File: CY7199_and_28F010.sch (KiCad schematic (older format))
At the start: 10 parts, among them U1 28F010, U10 74LS04, U11 74LS04, U2 28F010, U3 CY7C199, U4 CY7C199, U5 CY7C199, U6 CY7C199, U7 PAL16L8, U9 74LS04

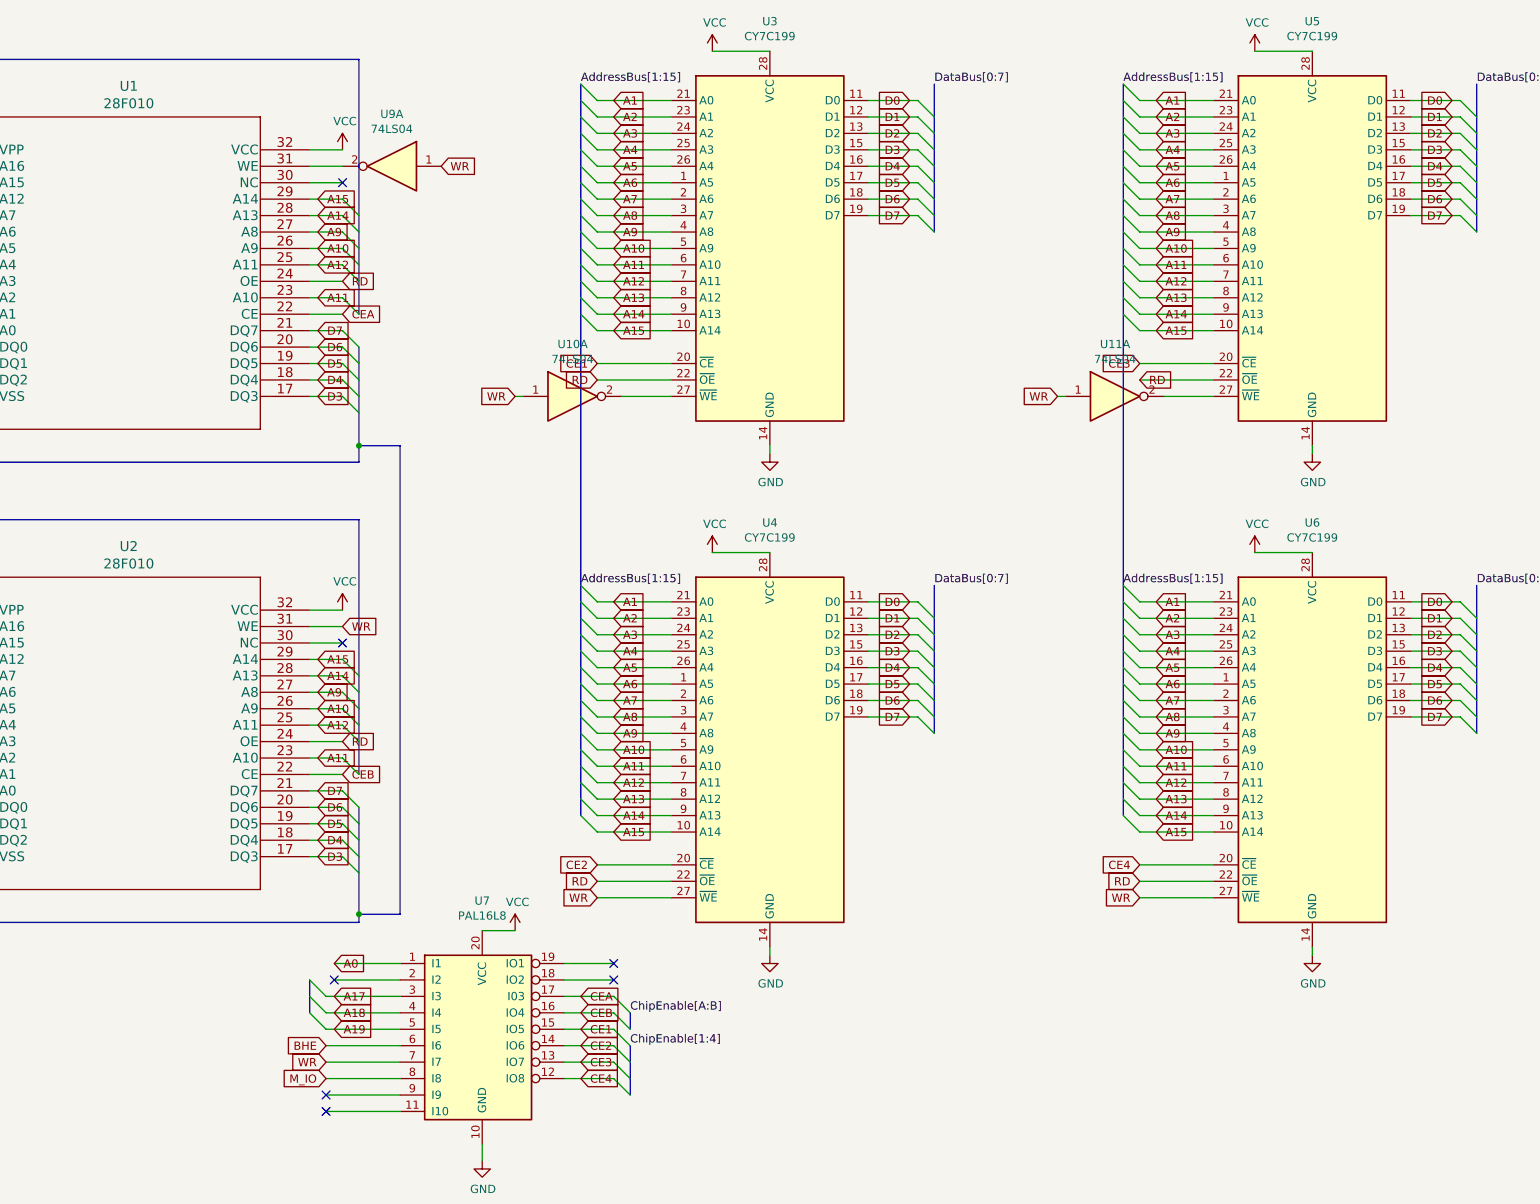
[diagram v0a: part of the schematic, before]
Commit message: tweeked cy7119_and_28f010.sch
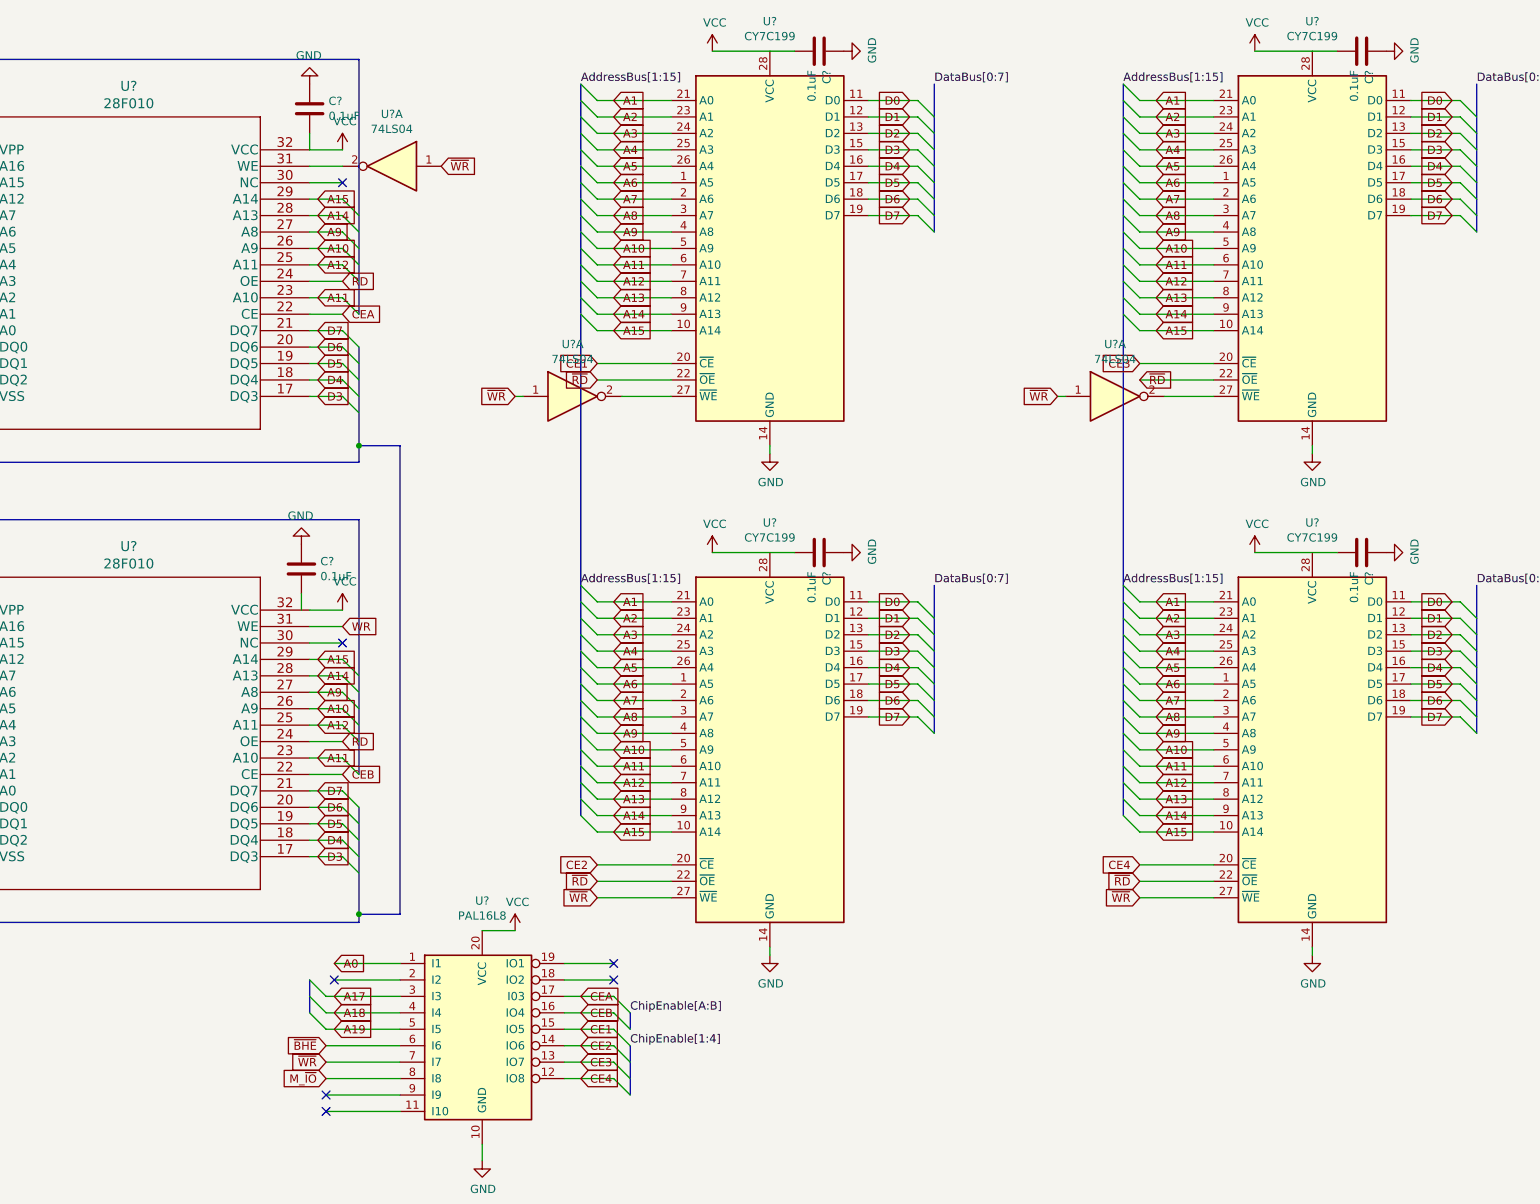
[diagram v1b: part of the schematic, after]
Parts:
- added C? (x6): 0.1uF, symbol Device:C
- renumbered U3 to U?, U7 to U?, U4 to U?, U2 to U?, U1 to U?, U5 to U?, U6 to U?, U11 to U?, U10 to U?, U9 to U?
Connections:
- net GND: now also C?.1, C?.1, C?.1, C?.1, C?.1, C?.1
- net RD: no longer U?.22 (~OE~), U?.22 (~OE~), U?.22 (~OE~), U?.22 (~OE~)
- net VCC: now also C?.2, C?.2, C?.2, C?.2, C?.2
- net WR: no longer U?.1, U?.1, U?.1, U?.27 (~WE~), U?.27 (~WE~), U?.7 (I7)
- net BHE renamed ~BHE
- net M_IO renamed M_~IO
- new net ~RD: U?.22 (~OE~), U?.22 (~OE~), U?.22 (~OE~), U?.22 (~OE~)
- new net ~WR: U?.1, U?.1, U?.1, U?.27 (~WE~), U?.27 (~WE~), U?.7 (I7)

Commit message: tweaked a few things
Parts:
- gave numbers to parts that had none: 16
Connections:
- net RD is gone; now on net ~RD: U601.24 (OE), U602.24 (OE)
- net WR is gone; now on net ~WR: U602.31 (WE)
- net VCC: now also C601.2
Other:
- moved on the sheet: C601
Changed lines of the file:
@@
 DataBus[0:7]
 $Comp
-L power:VCC #PWR?
+L power:VCC #PWR0157
 U 1 1 60912D5A
 P 3600 4250
-F 0 "#PWR?" H 3600 4100 50  0001 C CNN
+F 0 "#PWR0157" H 3600 4100 50  0001 C CNN
 F 1 "VCC" H 3615 4423 50  0000 C CNN
 F 2 "" H 3600 4250 50  0001 C CNN
@@
 $EndComp
 $Comp
-L power:GND #PWR?
+L power:GND #PWR0158
 U 1 1 609136CA
 P 1000 5750
-F 0 "#PWR?" H 1000 5500 50  0001 C CNN
+F 0 "#PWR0158" H 1000 5500 50  0001 C CNN
 F 1 "GND" H 1005 5577 50  0000 C CNN
 F 2 "" H 1000 5750 50  0001 C CNN
@@
 DataBus[0:7]
 $Comp
-L power:VCC #PWR?
+L power:VCC #PWR0159
 U 1 1 60989210
 P 3600 1450
-F 0 "#PWR?" H 3600 1300 50  0001 C CNN
+F 0 "#PWR0159" H 3600 1300 50  0001 C CNN
 F 1 "VCC" H 3615 1623 50  0000 C CNN
 F 2 "" H 3600 1450 50  0001 C CNN
@@
 $EndComp
 $Comp
-L power:GND #PWR?
+L power:GND #PWR0160
 U 1 1 60989216
 P 1000 2950
-F 0 "#PWR?" H 1000 2700 50  0001 C CNN
+F 0 "#PWR0160" H 1000 2700 50  0001 C CNN
 F 1 "GND" H 1005 2777 50  0000 C CNN
 F 2 "" H 1000 2950 50  0001 C CNN
@@
 	6200 6300 6200 6350
 $Comp
-L power:GND #PWR?
+L power:GND #PWR0161
 U 1 1 60C13B52
 P 6200 3300
-F 0 "#PWR?" H 6200 3050 50  0001 C CNN
+F 0 "#PWR0161" H 6200 3050 50  0001 C CNN
 F 1 "GND" H 6205 3127 50  0000 C CNN
 F 2 "" H 6200 3300 50  0001 C CNN
@@
 $EndComp
 $Comp
-L power:GND #PWR?
+L power:GND #PWR0162
 U 1 1 60C14372
 P 6200 6350
-F 0 "#PWR?" H 6200 6100 50  0001 C CNN
+F 0 "#PWR0162" H 6200 6100 50  0001 C CNN
 F 1 "GND" H 6205 6177 50  0000 C CNN
 F 2 "" H 6200 6350 50  0001 C CNN
@@
 	6200 850  5850 850
 $Comp
-L power:VCC #PWR?
+L power:VCC #PWR0163
 U 1 1 60C49E31
 P 5850 850
-F 0 "#PWR?" H 5850 700 50  0001 C CNN
+F 0 "#PWR0163" H 5850 700 50  0001 C CNN
 F 1 "VCC" H 5865 1023 50  0000 C CNN
 F 2 "" H 5850 850 50  0001 C CNN
@@
 $EndComp
 $Comp
-L power:VCC #PWR?
+L power:VCC #PWR0164
 U 1 1 60C4A9F7
 P 5850 3900
-F 0 "#PWR?" H 5850 3750 50  0001 C CNN
+F 0 "#PWR0164" H 5850 3750 50  0001 C CNN
 F 1 "VCC" H 5865 4073 50  0000 C CNN
 F 2 "" H 5850 3900 50  0001 C CNN
@@
 	9500 6300 9500 6350
 $Comp
-L power:GND #PWR?
+L power:GND #PWR0165
 U 1 1 60D25A8A
 P 9500 3300
-F 0 "#PWR?" H 9500 3050 50  0001 C CNN
+F 0 "#PWR0165" H 9500 3050 50  0001 C CNN
 F 1 "GND" H 9505 3127 50  0000 C CNN
 F 2 "" H 9500 3300 50  0001 C CNN
@@
 $EndComp
 $Comp
-L power:GND #PWR?
+L power:GND #PWR0166
 U 1 1 60D25A90
 P 9500 6350
-F 0 "#PWR?" H 9500 6100 50  0001 C CNN
+F 0 "#PWR0166" H 9500 6100 50  0001 C CNN
 F 1 "GND" H 9505 6177 50  0000 C CNN
 F 2 "" H 9500 6350 50  0001 C CNN
@@
 	9500 850  9150 850
 $Comp
-L power:VCC #PWR?
+L power:VCC #PWR0167
 U 1 1 60D25A98
 P 9150 850
-F 0 "#PWR?" H 9150 700 50  0001 C CNN
+F 0 "#PWR0167" H 9150 700 50  0001 C CNN
 F 1 "VCC" H 9165 1023 50  0000 C CNN
 F 2 "" H 9150 850 50  0001 C CNN
@@
 $EndComp
 $Comp
-L power:VCC #PWR?
+L power:VCC #PWR0168
 U 1 1 60D25A9E
 P 9150 3900
-F 0 "#PWR?" H 9150 3750 50  0001 C CNN
+F 0 "#PWR0168" H 9150 3750 50  0001 C CNN
 F 1 "VCC" H 9165 4073 50  0000 C CNN
 F 2 "" H 9150 3900 50  0001 C CNN
@@
 ~RD
 Text GLabel 3600 2250 2    50   Input ~ 0
-RD
+~RD
 Text GLabel 3600 5050 2    50   Input ~ 0
-RD
+~RD
 NoConn ~ 1000 1450
 NoConn ~ 1000 4250
 $Comp
-L Memory_RAM:CY7C199 U?
+L Memory_RAM:CY7C199 U610
 U 1 1 60D25A72
 P 9500 5100
-F 0 "U?" H 9500 6481 50  0000 C CNN
+F 0 "U610" H 9500 6481 50  0000 C CNN
 F 1 "CY7C199" H 9500 6390 50  0000 C CNN
 F 2 "" H 9500 5100 50  0001 C CNN
@@
 $EndComp
 $Comp
-L Memory_RAM:CY7C199 U?
+L Memory_RAM:CY7C199 U609
 U 1 1 60D259E8
 P 9500 2050
-F 0 "U?" H 9500 3431 50  0000 C CNN
+F 0 "U609" H 9500 3431 50  0000 C CNN
 F 1 "CY7C199" H 9500 3340 50  0000 C CNN
 F 2 "" H 9500 2050 50  0001 C CNN
@@
 $EndComp
 $Comp
-L Memory_RAM:CY7C199 U?
+L Memory_RAM:CY7C199 U607
 U 1 1 6081B573
 P 6200 5100
-F 0 "U?" H 6200 6481 50  0000 C CNN
+F 0 "U607" H 6200 6481 50  0000 C CNN
 F 1 "CY7C199" H 6200 6390 50  0000 C CNN
 F 2 "" H 6200 5100 50  0001 C CNN
@@
 $EndComp
 $Comp
-L Memory_RAM:CY7C199 U?
+L Memory_RAM:CY7C199 U606
 U 1 1 6078FC09
 P 6200 2050
-F 0 "U?" H 6200 3431 50  0000 C CNN
+F 0 "U606" H 6200 3431 50  0000 C CNN
 F 1 "CY7C199" H 6200 3340 50  0000 C CNN
 F 2 "" H 6200 2050 50  0001 C CNN
@@
 $EndComp
 $Comp
-L 28F010:28F010 U?
+L 28F010:28F010 U602
 U 1 1 608BE934
 P 1200 4250
-F 0 "U?" H 2300 4637 60  0000 C CNN
+F 0 "U602" H 2300 4637 60  0000 C CNN
 F 1 "28F010" H 2300 4531 60  0000 C CNN
 F 2 "28F010" H 2300 4490 60  0001 C CNN
@@
 $EndComp
 $Comp
-L 28F010:28F010 U?
+L 28F010:28F010 U601
 U 1 1 609891ED
 P 1200 1450
-F 0 "U?" H 2300 1837 60  0000 C CNN
+F 0 "U601" H 2300 1837 60  0000 C CNN
 F 1 "28F010" H 2300 1731 60  0000 C CNN
 F 2 "28F010" H 2300 1690 60  0001 C CNN
@@
 	4950 6500 5250 6500
 $Comp
-L power:VCC #PWR?
+L power:VCC #PWR0169
 U 1 1 60C816AC
 P 4650 6200
-F 0 "#PWR?" H 4650 6050 50  0001 C CNN
+F 0 "#PWR0169" H 4650 6050 50  0001 C CNN
 F 1 "VCC" H 4665 6373 50  0000 C CNN
 F 2 "" H 4650 6200 50  0001 C CNN
@@
 	4450 6200 4650 6200
 $Comp
-L power:GND #PWR?
+L power:GND #PWR0170
 U 1 1 609E86E1
 P 4450 7600
-F 0 "#PWR?" H 4450 7350 50  0001 C CNN
+F 0 "#PWR0170" H 4450 7350 50  0001 C CNN
 F 1 "GND" H 4455 7427 50  0000 C CNN
 F 2 "" H 4450 7600 50  0001 C CNN
@@
 	4450 7500 4450 7600
 $Comp
-L Logic_Programmable:PAL16L8 U?
+L Logic_Programmable:PAL16L8 U604
 U 1 1 6079CE46
 P 4450 6900
-F 0 "U?" H 4450 7781 50  0000 C CNN
+F 0 "U604" H 4450 7781 50  0000 C CNN
 F 1 "PAL16L8" H 4450 7690 50  0000 C CNN
 F 2 "" H 4450 6900 50  0001 C CNN
@@
 	5600 2950 5300 2950
 $Comp
-L 74xx:74LS04 U?
+L 74xx:74LS04 U605
 U 1 1 60EB960C
 P 5000 2950
-F 0 "U?" H 5000 3267 50  0000 C CNN
+F 0 "U605" H 5000 3267 50  0000 C CNN
 F 1 "74LS04" H 5000 3176 50  0000 C CNN
 F 2 "" H 5000 2950 50  0001 C CNN
@@
 D7
 Text GLabel 3600 4350 2    50   Input ~ 0
-WR
+~WR
 Text GLabel 8550 4200 2    50   Input ~ 0
 A1
@@
 	8000 2950 7950 2950
 $Comp
-L 74xx:74LS04 U?
+L 74xx:74LS04 U608
 U 1 1 60DAFE04
 P 8300 2950
-F 0 "U?" H 8300 3267 50  0000 C CNN
+F 0 "U608" H 8300 3267 50  0000 C CNN
 F 1 "74LS04" H 8300 3176 50  0000 C CNN
 F 2 "" H 8300 2950 50  0001 C CNN
@@
 $EndComp
 $Comp
-L 74xx:74LS04 U?
+L 74xx:74LS04 U603
 U 1 1 60F155ED
 P 3900 1550
-F 0 "U?" H 3900 1867 50  0000 C CNN
+F 0 "U603" H 3900 1867 50  0000 C CNN
 F 1 "74LS04" H 3900 1776 50  0000 C CNN
 F 2 "" H 3900 1550 50  0001 C CNN
@@
 	6200 850  6350 850
 $Comp
-L Device:C C?
+L Device:C C603
 U 1 1 60ACE147
 P 6500 850
-F 0 "C?" H 6615 896 50  0000 L CNN
+F 0 "C603" H 6615 896 50  0000 L CNN
 F 1 "0.1uF" H 6615 805 50  0000 L CNN
 F 2 "" H 6538 700 50  0001 C CNN
@@
 $EndComp
 $Comp
-L power:GND #PWR?
+L power:GND #PWR0171
 U 1 1 60ACE14D
 P 6650 850
-F 0 "#PWR?" H 6650 600 50  0001 C CNN
+F 0 "#PWR0171" H 6650 600 50  0001 C CNN
 F 1 "GND" H 6655 677 50  0000 C CNN
 F 2 "" H 6650 850 50  0001 C CNN
@@
 	9500 850  9650 850
 $Comp
-L Device:C C?
+L Device:C C605
 U 1 1 60AE6CDD
 P 9800 850
-F 0 "C?" H 9915 896 50  0000 L CNN
+F 0 "C605" H 9915 896 50  0000 L CNN
 F 1 "0.1uF" H 9915 805 50  0000 L CNN
 F 2 "" H 9838 700 50  0001 C CNN
@@
 $EndComp
 $Comp
-L power:GND #PWR?
+L power:GND #PWR0172
 U 1 1 60AE6CE3
 P 9950 850
-F 0 "#PWR?" H 9950 600 50  0001 C CNN
+F 0 "#PWR0172" H 9950 600 50  0001 C CNN
 F 1 "GND" H 9955 677 50  0000 C CNN
 F 2 "" H 9950 850 50  0001 C CNN
@@
 	6200 3900 6350 3900
 $Comp
-L Device:C C?
+L Device:C C604
 U 1 1 60AFEE60
 P 6500 3900
-F 0 "C?" H 6615 3946 50  0000 L CNN
+F 0 "C604" H 6615 3946 50  0000 L CNN
 F 1 "0.1uF" H 6615 3855 50  0000 L CNN
 F 2 "" H 6538 3750 50  0001 C CNN
@@
 $EndComp
 $Comp
-L power:GND #PWR?
+L power:GND #PWR0173
 U 1 1 60AFEE66
 P 6650 3900
-F 0 "#PWR?" H 6650 3650 50  0001 C CNN
+F 0 "#PWR0173" H 6650 3650 50  0001 C CNN
 F 1 "GND" H 6655 3727 50  0000 C CNN
 F 2 "" H 6650 3900 50  0001 C CNN
@@
 	9500 3900 9650 3900
 $Comp
-L Device:C C?
+L Device:C C606
 U 1 1 60B17659
 P 9800 3900
-F 0 "C?" H 9915 3946 50  0000 L CNN
+F 0 "C606" H 9915 3946 50  0000 L CNN
 F 1 "0.1uF" H 9915 3855 50  0000 L CNN
 F 2 "" H 9838 3750 50  0001 C CNN
@@
 $EndComp
 $Comp
-L power:GND #PWR?
+L power:GND #PWR0174
 U 1 1 60B1765F
 P 9950 3900
-F 0 "#PWR?" H 9950 3650 50  0001 C CNN
+F 0 "#PWR0174" H 9950 3650 50  0001 C CNN
 F 1 "GND" H 9955 3727 50  0000 C CNN
 F 2 "" H 9950 3900 50  0001 C CNN
@@
 $EndComp
 $Comp
-L Device:C C?
+L Device:C C601
 U 1 1 60B481A0
-P 3350 4000
-F 0 "C?" H 3465 4046 50  0000 L CNN
-F 1 "0.1uF" H 3465 3955 50  0000 L CNN
-F 2 "" H 3388 3850 50  0001 C CNN
-F 3 "~" H 3350 4000 50  0001 C CNN
-	1    3350 4000
-	1    0    0    -1
-$EndComp
-$Comp
-L power:GND #PWR?
+P 3400 3950
+F 0 "C601" H 3515 3996 50  0000 L CNN
+F 1 "0.1uF" H 3515 3905 50  0000 L CNN
+F 2 "" H 3438 3800 50  0001 C CNN
+F 3 "~" H 3400 3950 50  0001 C CNN
+	1    3400 3950
+	1    0    0    -1
+$EndComp
+$Comp
+L power:GND #PWR0175
 U 1 1 60B481A6
-P 3350 3850
-F 0 "#PWR?" H 3350 3600 50  0001 C CNN
-F 1 "GND" H 3355 3677 50  0000 C CNN
-F 2 "" H 3350 3850 50  0001 C CNN
-F 3 "" H 3350 3850 50  0001 C CNN
-	1    3350 3850
+P 3400 3800
+F 0 "#PWR0175" H 3400 3550 50  0001 C CNN
+F 1 "GND" H 3405 3627 50  0000 C CNN
+F 2 "" H 3400 3800 50  0001 C CNN
+F 3 "" H 3400 3800 50  0001 C CNN
+	1    3400 3800
 	-1   0    0    1
 $EndComp
-Wire Wire Line
-	3350 4150 3350 4250
-$Comp
-L Device:C C?
+$Comp
+L Device:C C602
 U 1 1 60C0C861
 P 3400 1200
-F 0 "C?" H 3515 1246 50  0000 L CNN
+F 0 "C602" H 3515 1246 50  0000 L CNN
 F 1 "0.1uF" H 3515 1155 50  0000 L CNN
 F 2 "" H 3438 1050 50  0001 C CNN
@@
 $EndComp
 $Comp
-L power:GND #PWR?
+L power:GND #PWR0176
 U 1 1 60C0C867
 P 3400 1050
-F 0 "#PWR?" H 3400 800 50  0001 C CNN
+F 0 "#PWR0176" H 3400 800 50  0001 C CNN
 F 1 "GND" H 3405 877 50  0000 C CNN
 F 2 "" H 3400 1050 50  0001 C CNN
@@
 Wire Wire Line
 	3400 1350 3400 1450
+Wire Wire Line
+	3400 4100 3400 4250
+Connection ~ 3400 4250
 Wire Bus Line
 	3400 6500 3400 6700

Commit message: made final adjustments to all the designes
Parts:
- removed U605, U608: 74LS04, symbol 74xx:74LS04
- added unit 2 of U603
- added unit 3 of U603
- added unit 7 of U603
- C601: renamed from C602; footprint (none) -> Capacitor_SMD:CP_Elec_3x5.3
- C602: renamed from C601; footprint (none) -> Capacitor_SMD:CP_Elec_3x5.3
- C603, C604, C605, C606: footprint (none) -> Capacitor_SMD:CP_Elec_3x5.3
- U601, U602: footprint 28F010 -> parts:28F010
- U603: footprint (none) -> Package_DIP:DIP-14_W7.62mm_SMDSocket_SmallPads
- U604: footprint (none) -> Package_DIP:DIP-20_W7.62mm_SMDSocket_SmallPads
- U605: renamed from U606; footprint (none) -> Package_DIP:DIP-28_W7.62mm_SMDSocket_SmallPads
- U606: renamed from U607; footprint (none) -> Package_DIP:DIP-28_W7.62mm_SMDSocket_SmallPads
- U607: renamed from U609; footprint (none) -> Package_DIP:DIP-28_W7.62mm_SMDSocket_SmallPads
- U608: renamed from U610; footprint (none) -> Package_DIP:DIP-28_W7.62mm_SMDSocket_SmallPads
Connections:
- net GND: now also U603.7 (GND)
- net VCC: now also U603.14 (VCC)
- net ~WR: now also U603.3, U603.5
- net at U605.27 (~WE~): now also U603.4
- net at U607.27 (~WE~): now also U603.6
